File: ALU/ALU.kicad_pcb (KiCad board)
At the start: 2 copper layers, 79.5 x 43 mm, 26 parts, among them J1 Conn_01x04_Pin, J2 Conn_01x08_Pin, J3 Conn_01x08_Pin, J4 Conn_01x08_Socket, U1 SN74F86N, U2 SN74F86N, U3 SN74HCT245N, U4 CD74HCT283E, U5 CD74HCT283E

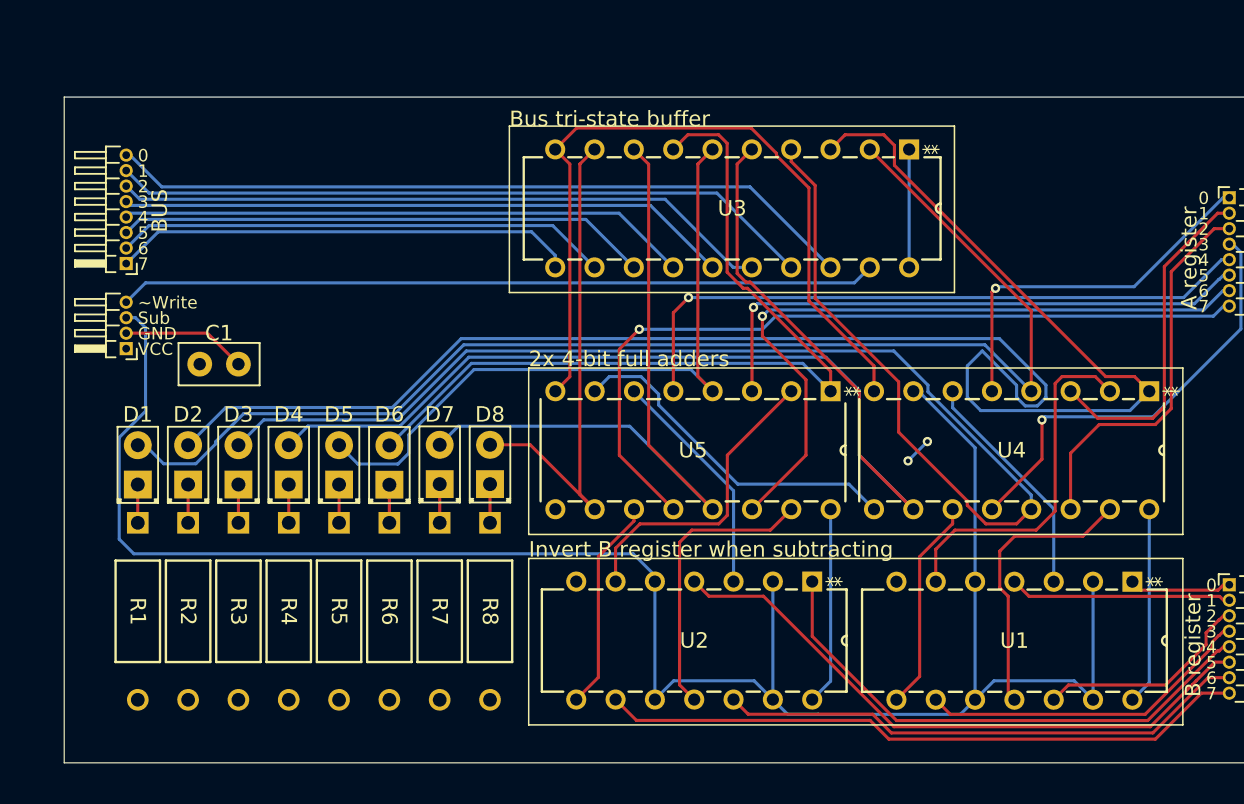
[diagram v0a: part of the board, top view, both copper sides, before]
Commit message: Switched LEDs to MSB first. Added label to board.
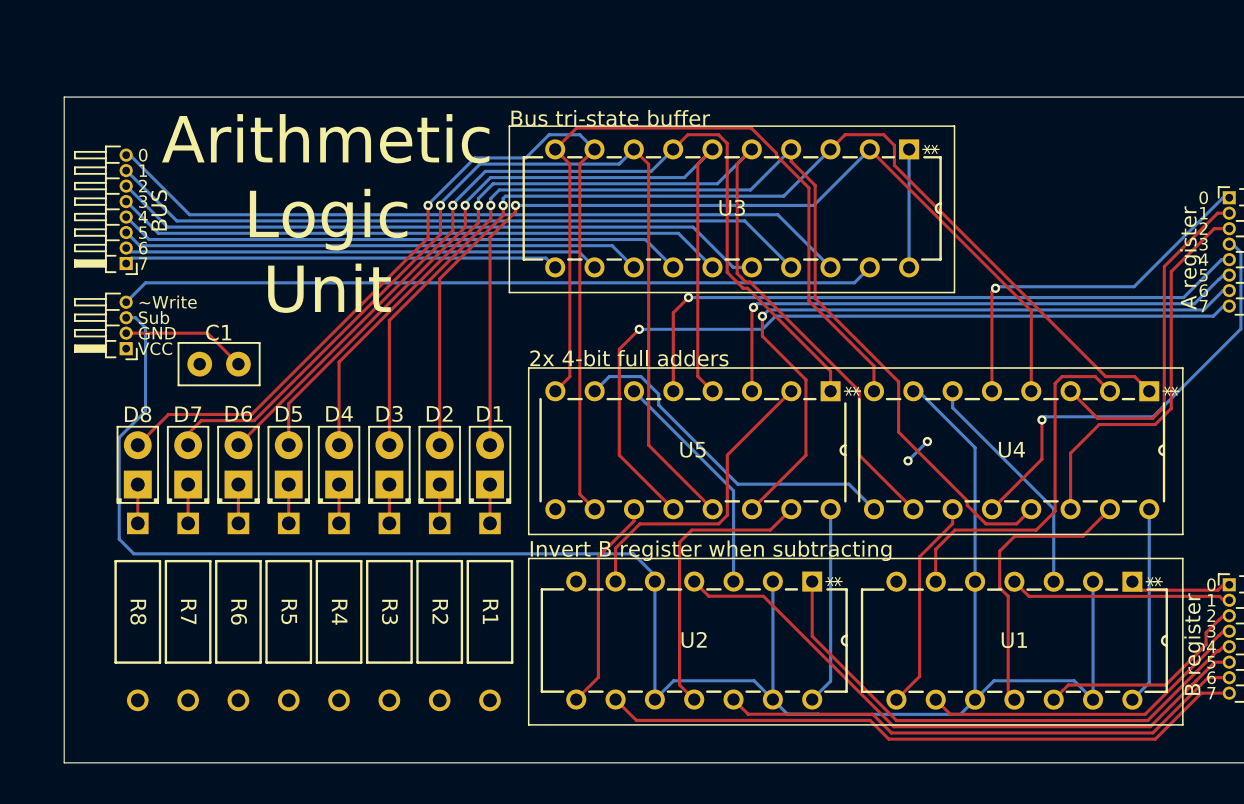
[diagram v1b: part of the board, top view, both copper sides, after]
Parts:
- moved R1 22.8 mm to (108.0, 127.5)
- moved R8 22.8 mm to (85.2, 127.5)
- moved D8 22.8 mm to (85.2, 125.0)
- moved D1 22.8 mm to (108.0, 125.0)
- moved R2 16.3 mm to (104.8, 127.5)
- moved R7 16.3 mm to (88.5, 127.5)
- moved D7 16.3 mm to (88.5, 125.0)
- moved D2 16.2 mm to (104.8, 125.0)
- moved R3 9.75 mm to (101.5, 127.5)
- moved R6 9.75 mm to (91.8, 127.5)
- moved D6 9.75 mm to (91.8, 125.0)
- moved D3 9.75 mm to (101.5, 125.0)
- moved R4 3.25 mm to (98.2, 127.5)
- moved R5 3.25 mm to (95.0, 127.5)
- moved D4 3.25 mm to (98.2, 125.0)
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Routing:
- net /S1: track 111.2 -> 68.7 mm, vias 0 -> 1
- net /S7: track 32.5 -> 63.5 mm, vias 0 -> 1
- net /S0: track 82.9 -> 60.5 mm, vias 0 -> 1
- net /S2: track 91.5 -> 72.1 mm, vias 0 -> 1
- net /S6: track 45.7 -> 63.6 mm, vias 0 -> 1
- net /S3: track 77.7 -> 67.1 mm, vias 0 -> 1
- net /S4: track 44.8 -> 54.2 mm, vias 0 -> 1
- net /S5: track 54.9 -> 60.5 mm, vias 0 -> 1
- net Net-(J4-Pin_1): track 30.0 -> 28.1 mm
- net Net-(J4-Pin_2): track 32.0 -> 30.8 mm
- net Net-(J4-Pin_3): track 34.4 -> 33.7 mm
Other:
- board text added: "Arithmetic Logic Unit"

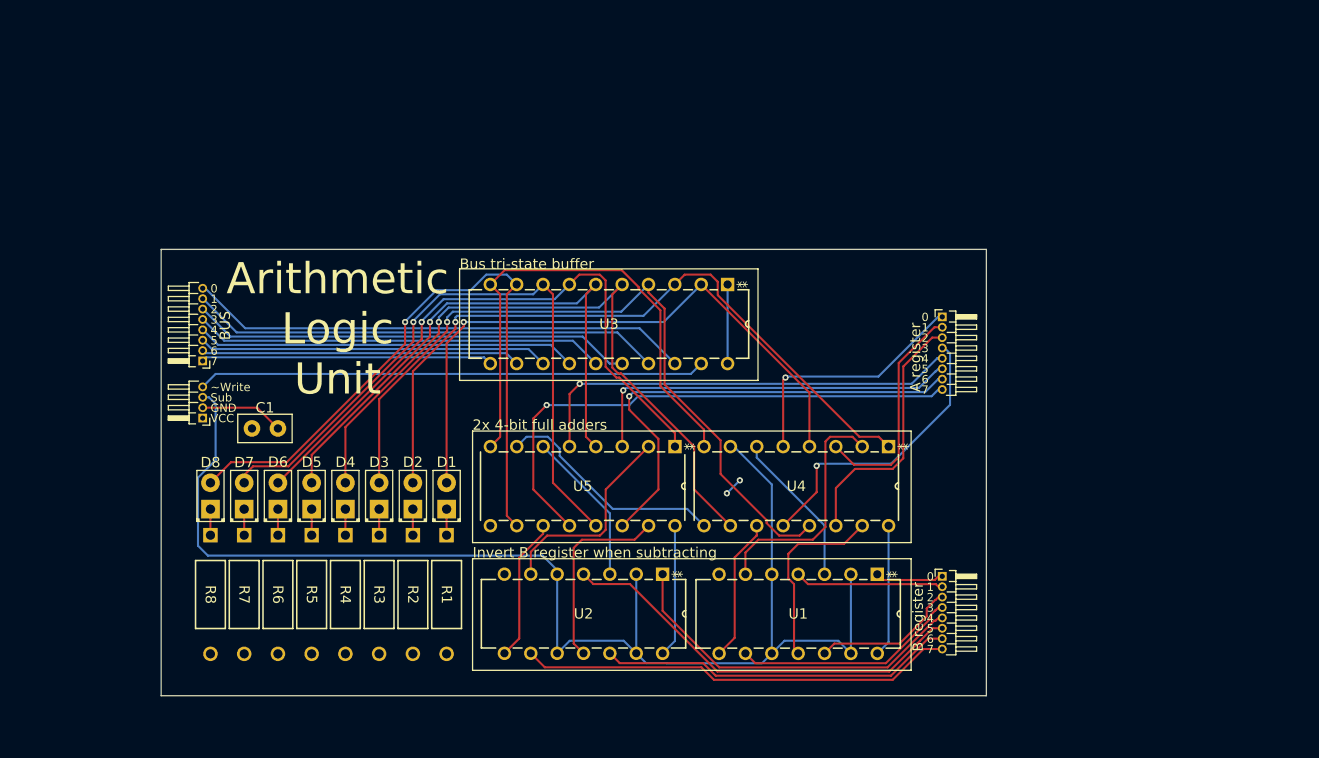
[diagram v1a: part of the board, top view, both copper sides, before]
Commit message: Addded ALU flags register and laided out the PCB again
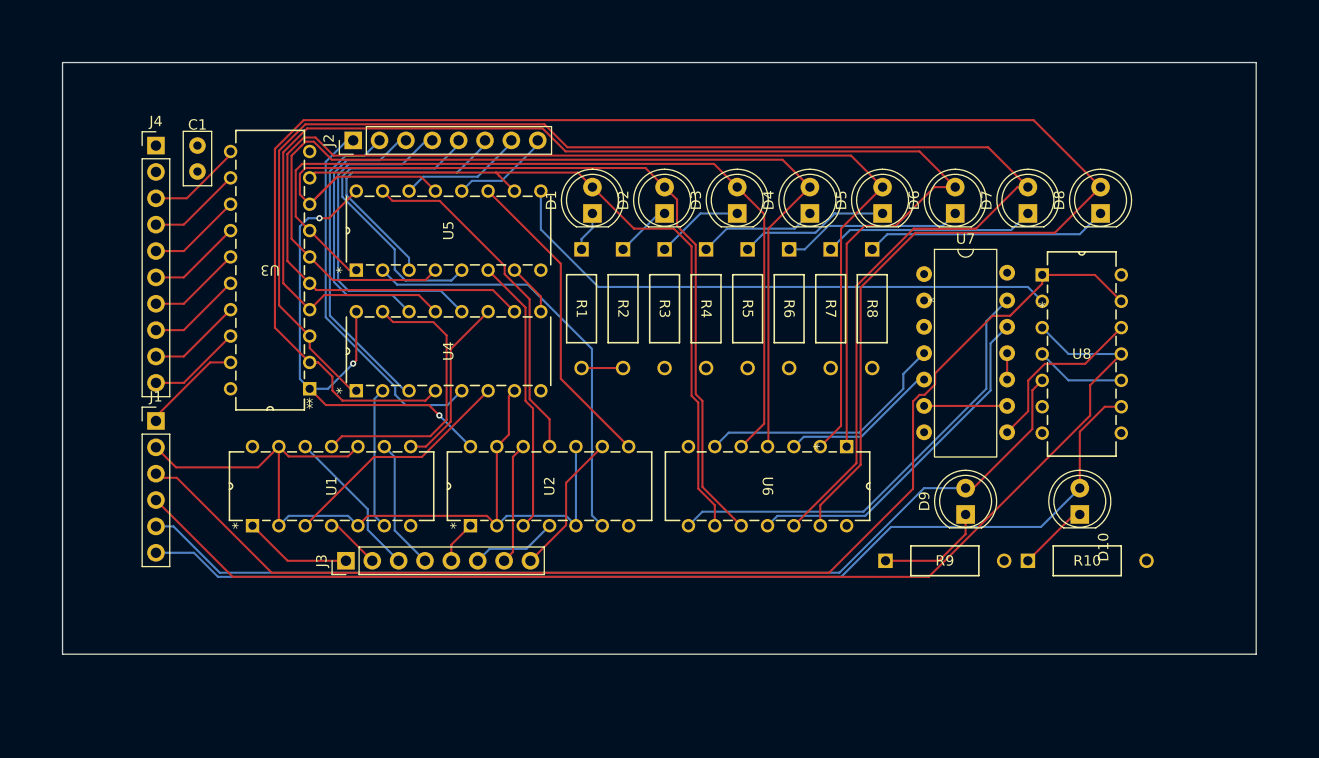
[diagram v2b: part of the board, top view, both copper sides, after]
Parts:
- added D10: LED, LED_THT:LED_D5.0mm, F.Cu at (169.0, 125.5)
- added D9: LED, LED_THT:LED_D5.0mm, F.Cu at (158.0, 125.5)
- added R10: 220, _DownloadFootprints:CF_series_Resistors_THT, F.Cu at (164.0, 130.0)
- added R9: 220, _DownloadFootprints:CF_series_Resistors_THT, F.Cu at (150.3, 130.0)
- added U6: SN74F86N, _DownloadFootprints:4x_nor, F.Cu at (131.3, 126.6)
- added U7: ~, 8BitCPUFootprints:4x_and, F.Cu at (158.0, 110.0)
- added U8: Dual D FF, _DownloadFootprints:2x_D_FF, F.Cu at (173.0, 117.7)
- D1, D2, D3, D4, D5, D6, D7, D8: footprint LED_THT:LED_D2.0mm_W4.8mm_H2.5mm_FlatTop -> LED_THT:LED_D5.0mm
- J1: value Conn_01x04_Pin -> Conn_01x06_Pin; footprint Connector_PinHeader_1.00mm:PinHeader_1x04_P1.00mm_Horizontal -> Connector_PinHeader_2.54mm:PinHeader_1x06_P2.54mm_Vertical
- J2, J3: footprint Connector_PinHeader_1.00mm:PinHeader_1x08_P1.00mm_Horizontal -> Connector_PinHeader_2.54mm:PinHeader_1x08_P2.54mm_Vertical
- J4: value Conn_01x08_Socket -> Conn_01x10_Pin; footprint Connector_PinHeader_1.00mm:PinHeader_1x08_P1.00mm_Horizontal -> Connector_PinHeader_2.54mm:PinHeader_1x10_P2.54mm_Vertical
- moved D8 90.4 mm to (171.0, 96.5)
- moved D7 80.7 mm to (164.0, 96.5)
- moved D6 71.2 mm to (157.0, 96.5)
- moved R8 69.4 mm to (149.0, 100.0)
- moved R7 62.9 mm to (145.0, 100.0)
- moved D5 61.9 mm to (150.0, 96.5)
- moved J2 59.2 mm to (99.0, 89.5), turned to 90 degrees
- moved J3 57.5 mm to (98.3, 130.0), turned to 90 degrees
- moved R6 56.4 mm to (141.0, 100.0)
- moved D4 53.0 mm to (143.0, 96.5)
- moved R5 50.2 mm to (137.0, 100.0)
- moved D3 44.7 mm to (136.0, 96.5)
- moved R4 44.3 mm to (133.0, 100.0)
- moved R3 38.9 mm to (129.0, 100.0)
- moved D2 37.4 mm to (129.0, 96.5)
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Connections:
- D1 pad 2: /S0 -> /S7
- D2 pad 2: /S1 -> /S6
- D3 pad 2: /S2 -> /S5
- D4 pad 2: /S3 -> /S4
- D5 pad 2: /S4 -> /S3
- D6 pad 2: /S5 -> /S2
- D7 pad 2: /S6 -> /S1
- D8 pad 2: /S7 -> /S0
- J1 pad 1: +5V -> /~{WRITE}
- J1 pad 2: GND -> /Subtract
- J1 pad 3: /Subtract -> /~{RST}
- J1 pad 4: /~WRITE -> /CLK
- J4 pad 1: Net-(J4-Pin_1) -> +5V
- J4 pad 2: Net-(J4-Pin_2) -> GND
- U3 pad 11: Net-(J4-Pin_1) -> Net-(J4-Pin_3)
- U3 pad 12: Net-(J4-Pin_2) -> Net-(J4-Pin_4)
- U3 pad 13: Net-(J4-Pin_3) -> Net-(J4-Pin_5)
- U3 pad 14: Net-(J4-Pin_4) -> Net-(J4-Pin_6)
- U3 pad 15: Net-(J4-Pin_5) -> Net-(J4-Pin_7)
- U3 pad 16: Net-(J4-Pin_6) -> Net-(J4-Pin_8)
- U3 pad 17: Net-(J4-Pin_7) -> Net-(J4-Pin_9)
- U3 pad 18: Net-(J4-Pin_8) -> Net-(J4-Pin_10)
- U3 pad 19: /~WRITE -> /~{WRITE}
- U5 pad 9: unconnected-(U5-COUT-Pad9) -> /FlagsRegister/Carry
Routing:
- net /~{RST}: track 0.00 -> 115.9 mm
- net /CLK: track 0.00 -> 115.3 mm
- net /S0: track 60.5 -> 171.8 mm, vias 1 -> 0
- net /ZERO: track 0.00 -> 103.9 mm
- net /CARRY: track 0.00 -> 97.1 mm
- net /S1: track 68.7 -> 147.8 mm, vias 1 -> 0
- net /S2: track 72.1 -> 129.9 mm, vias 1 -> 0
- net /FlagsRegister/Carry: track 0.00 -> 54.9 mm
- net /S3: track 67.1 -> 121.7 mm, vias 1 -> 0
- net GND: track 58.0 -> 4.00 mm
- net /~WRITE: track 49.0 -> 0.00 mm
- net /S4: track 54.2 -> 102.9 mm, vias 1 -> 0
- net /Subtract: track 127.3 -> 81.8 mm
- net Net-(U6-3Y): track 0.00 -> 43.5 mm
- net /A7: track 52.0 -> 9.59 mm, vias 1 -> 0
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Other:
- board size 79.5 x 43 mm -> 115 x 57 mm
- board text removed: "0"
- board text removed: "1"
- board text removed: "2"
- board text removed: "2x 4-bit full adders"
- board text removed: "3"
- board text removed: "4"
- board text removed: "5"
- board text removed: "6"
- board text removed: "7"
- board text removed: "A register"
- board text removed: "Arithmetic Logic Unit"
- board text removed: "B register"
- board text removed: "BUS"
- board text removed: "Bus tri-state buffer"
- board text removed: "GND"
- board text removed: "Invert B register when subtracting"
- board text removed: "Sub"
- board text removed: "VCC"
- board text removed: "~Write"

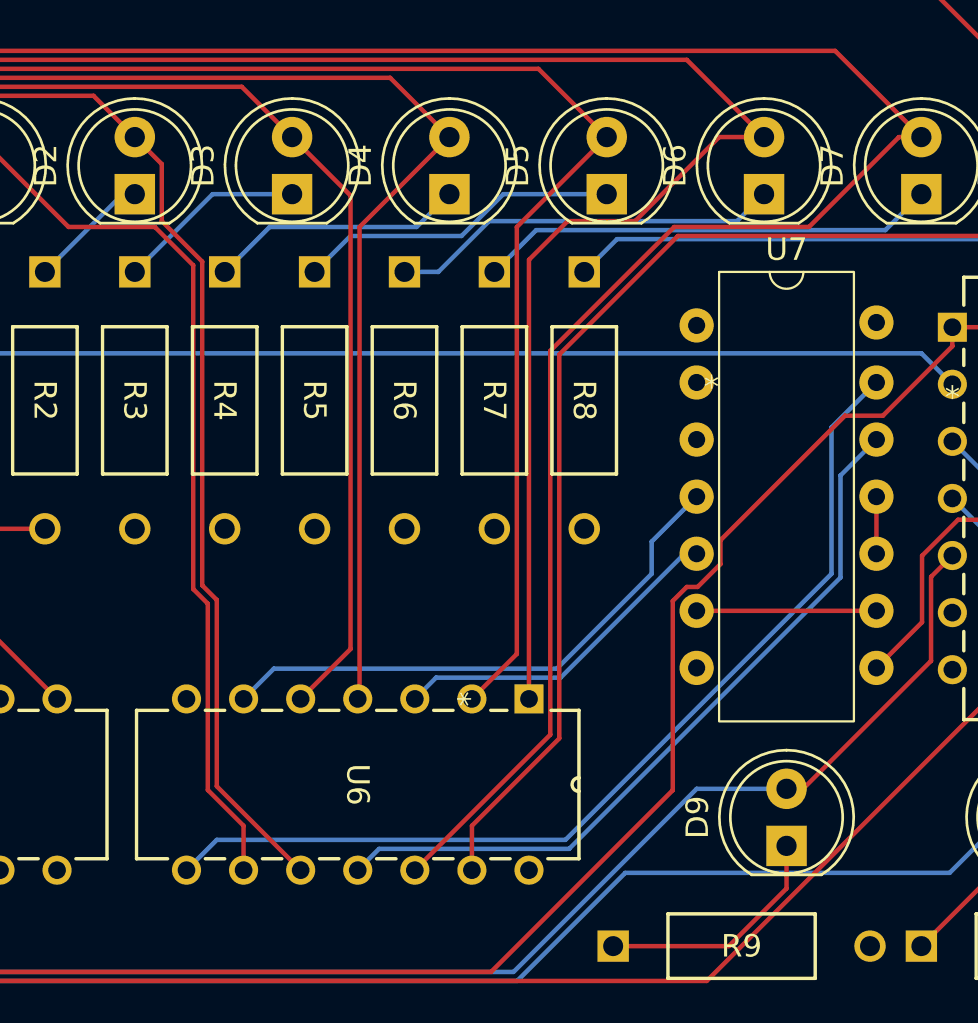
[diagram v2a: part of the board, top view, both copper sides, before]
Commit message: 4x NOR pinout was wrong. Updated with correct pinout. Fixed 2x D flip-flop references
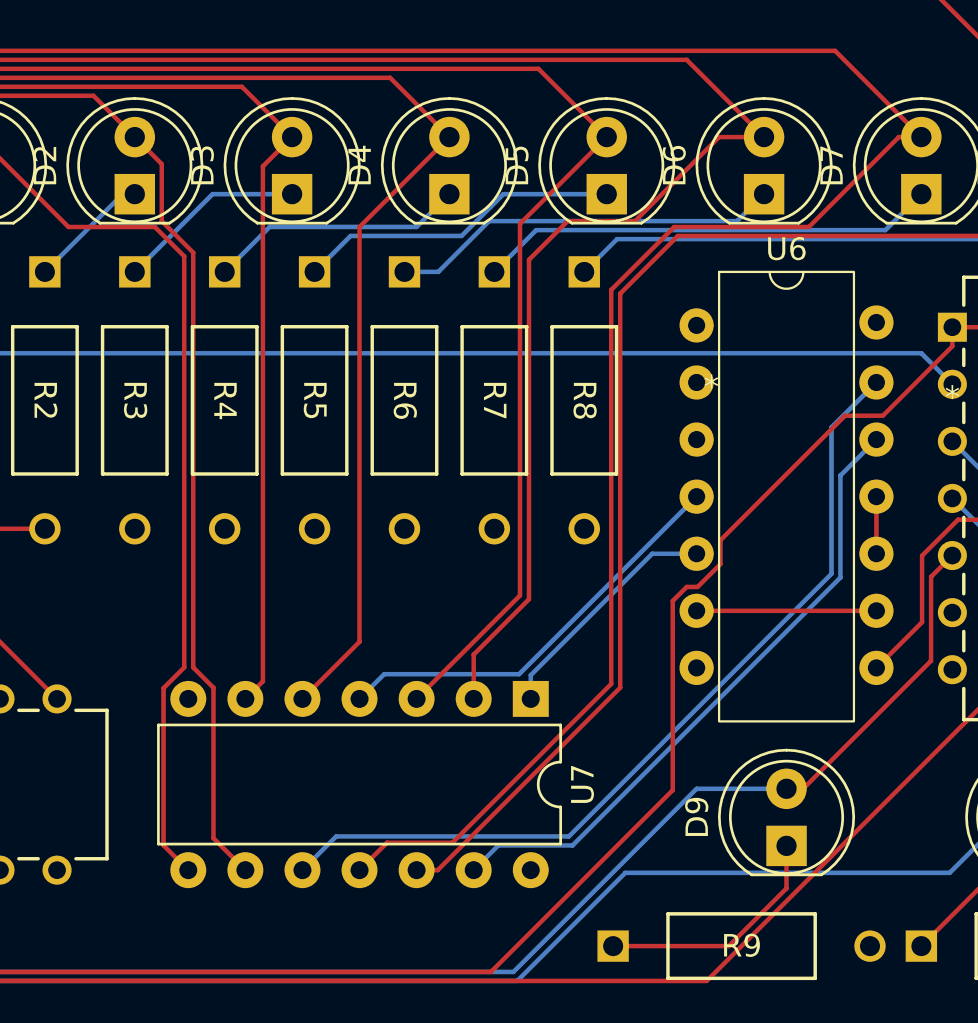
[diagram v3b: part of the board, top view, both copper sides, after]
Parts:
- removed the U6 at (131.3, 126.6)
- added U7: ~, Package_DIP:DIP-14_W7.62mm, F.Cu at (146.6, 119.0)
- renumbered U7 to U6
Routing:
- net Net-(U6-2A): track 24.7 -> 18.7 mm
- net Net-(U6-4A): track 33.7 -> 28.5 mm
- net Net-(U6-4B): track 43.5 -> 38.3 mm
- net Net-(U6-2B): track 15.2 -> 10.7 mm
- net /S1: track 147.8 -> 150.5 mm
- net /S0: track 171.8 -> 173.4 mm
- net /S5: track 83.1 -> 82.0 mm
- net /S6: track 92.7 -> 91.6 mm
- net /S3: track 121.7 -> 122.7 mm
- net /S2: track 129.9 -> 130.9 mm
- net /S4: track 102.9 -> 103.9 mm

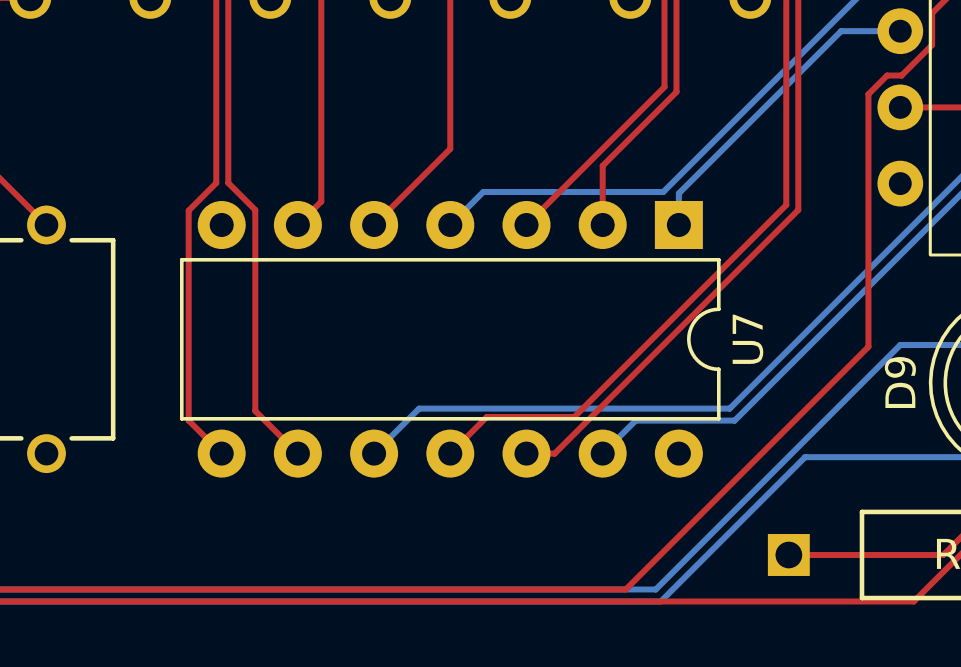
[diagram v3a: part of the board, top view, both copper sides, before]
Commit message: Fixed NOR schematic labeled as OR in ALU
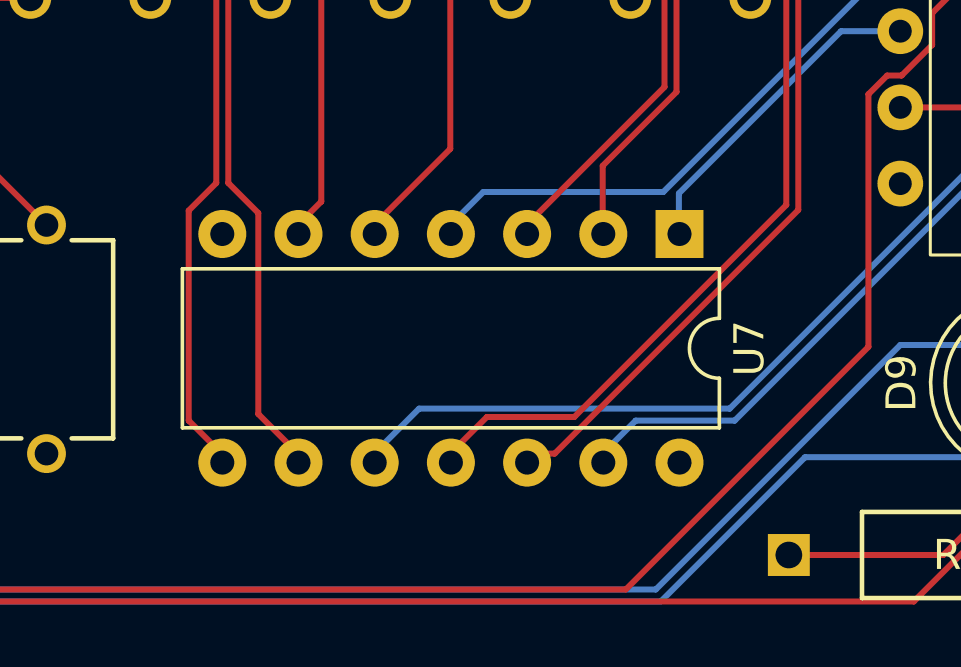
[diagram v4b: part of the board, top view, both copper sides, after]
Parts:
- moved U7 0.30 mm to (146.6, 119.3)
